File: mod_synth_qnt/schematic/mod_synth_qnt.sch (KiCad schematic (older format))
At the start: 37 parts, among them J1 CV IN, J2 Conn_02x08_Odd_Even, J3 QUANTIZE OUT, J4 Conn_01x07_Male, J5 Conn_01x07_Female, J6 Conn_01x07_Female, J7 Conn_01x07_Male, U1 LM358

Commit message: Use 3mm LEDs for panel hole clearance
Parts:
- D10, D11, D12, D13, D2, D3, D4, D5, D6, D7, D8, D9: footprint LED_THT:LED_D5.0mm -> LED_THT:LED_D3.0mm
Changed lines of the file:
@@
 F 0 "D2" V 8272 2779 50  0000 L CNN
 F 1 "LED 3" V 8363 2779 50  0000 L CNN
-F 2 "LED_THT:LED_D5.0mm" H 8325 2700 50  0001 C CNN
+F 2 "LED_THT:LED_D3.0mm" H 8325 2700 50  0001 C CNN
 F 3 "~" H 8325 2700 50  0001 C CNN
 	1    8325 2700
@@
 F 0 "D3" V 8272 3304 50  0000 L CNN
 F 1 "LED 7" V 8363 3304 50  0000 L CNN
-F 2 "LED_THT:LED_D5.0mm" H 8325 3225 50  0001 C CNN
+F 2 "LED_THT:LED_D3.0mm" H 8325 3225 50  0001 C CNN
 F 3 "~" H 8325 3225 50  0001 C CNN
 	1    8325 3225
@@
 F 0 "D4" V 8272 3829 50  0000 L CNN
 F 1 "LED 11" V 8363 3829 50  0000 L CNN
-F 2 "LED_THT:LED_D5.0mm" H 8325 3750 50  0001 C CNN
+F 2 "LED_THT:LED_D3.0mm" H 8325 3750 50  0001 C CNN
 F 3 "~" H 8325 3750 50  0001 C CNN
 	1    8325 3750
@@
 F 0 "D8" V 8972 2779 50  0000 L CNN
 F 1 "LED 6" V 9063 2779 50  0000 L CNN
-F 2 "LED_THT:LED_D5.0mm" H 9025 2700 50  0001 C CNN
+F 2 "LED_THT:LED_D3.0mm" H 9025 2700 50  0001 C CNN
 F 3 "~" H 9025 2700 50  0001 C CNN
 	1    9025 2700
@@
 F 0 "D10" V 9547 3804 50  0000 L CNN
 F 1 "LED 10" V 9638 3804 50  0000 L CNN
-F 2 "LED_THT:LED_D5.0mm" H 9600 3725 50  0001 C CNN
+F 2 "LED_THT:LED_D3.0mm" H 9600 3725 50  0001 C CNN
 F 3 "~" H 9600 3725 50  0001 C CNN
 	1    9600 3725
@@
 F 0 "D12" V 10022 3304 50  0000 L CNN
 F 1 "LED 9" V 10113 3304 50  0000 L CNN
-F 2 "LED_THT:LED_D5.0mm" H 10075 3225 50  0001 C CNN
+F 2 "LED_THT:LED_D3.0mm" H 10075 3225 50  0001 C CNN
 F 3 "~" H 10075 3225 50  0001 C CNN
 	1    10075 3225
@@
 F 0 "D13" V 10514 3107 50  0000 R CNN
 F 1 "LED 2" V 10423 3107 50  0000 R CNN
-F 2 "LED_THT:LED_D5.0mm" H 10475 3225 50  0001 C CNN
+F 2 "LED_THT:LED_D3.0mm" H 10475 3225 50  0001 C CNN
 F 3 "~" H 10475 3225 50  0001 C CNN
 	1    10475 3225
@@
 F 0 "D5" V 8689 2582 50  0000 R CNN
 F 1 "LED 0" V 8598 2582 50  0000 R CNN
-F 2 "LED_THT:LED_D5.0mm" H 8650 2700 50  0001 C CNN
+F 2 "LED_THT:LED_D3.0mm" H 8650 2700 50  0001 C CNN
 F 3 "~" H 8650 2700 50  0001 C CNN
 	1    8650 2700
@@
 F 0 "D6" V 8689 3082 50  0000 R CNN
 F 1 "LED 4" V 8598 3082 50  0000 R CNN
-F 2 "LED_THT:LED_D5.0mm" H 8650 3200 50  0001 C CNN
+F 2 "LED_THT:LED_D3.0mm" H 8650 3200 50  0001 C CNN
 F 3 "~" H 8650 3200 50  0001 C CNN
 	1    8650 3200
@@
 F 0 "D7" V 8689 3657 50  0000 R CNN
 F 1 "LED 8" V 8598 3657 50  0000 R CNN
-F 2 "LED_THT:LED_D5.0mm" H 8650 3775 50  0001 C CNN
+F 2 "LED_THT:LED_D3.0mm" H 8650 3775 50  0001 C CNN
 F 3 "~" H 8650 3775 50  0001 C CNN
 	1    8650 3775
@@
 F 0 "D9" V 9289 2582 50  0000 R CNN
 F 1 "LED 1" V 9198 2582 50  0000 R CNN
-F 2 "LED_THT:LED_D5.0mm" H 9250 2700 50  0001 C CNN
+F 2 "LED_THT:LED_D3.0mm" H 9250 2700 50  0001 C CNN
 F 3 "~" H 9250 2700 50  0001 C CNN
 	1    9250 2700
@@
 F 0 "D11" V 9864 3607 50  0000 R CNN
 F 1 "LED 5" V 9773 3607 50  0000 R CNN
-F 2 "LED_THT:LED_D5.0mm" H 9825 3725 50  0001 C CNN
+F 2 "LED_THT:LED_D3.0mm" H 9825 3725 50  0001 C CNN
 F 3 "~" H 9825 3725 50  0001 C CNN
 	1    9825 3725

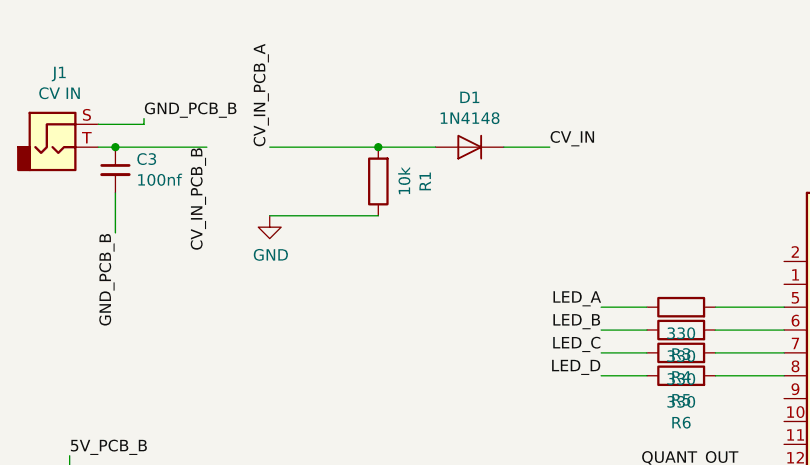
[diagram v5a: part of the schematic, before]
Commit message: Update resistor options
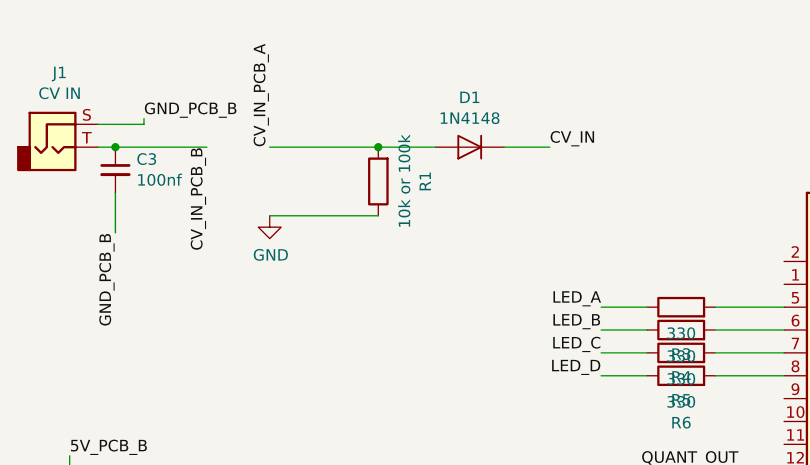
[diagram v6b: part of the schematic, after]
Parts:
- R1: value 10k -> 10k or 100k
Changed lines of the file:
@@
 P 2375 1150
 F 0 "R1" V 2168 1150 50  0000 C CNN
-F 1 "10k" V 2259 1150 50  0000 C CNN
+F 1 "10k or 100k" V 2259 1150 50  0000 C CNN
 F 2 "Resistor_THT:R_Axial_DIN0207_L6.3mm_D2.5mm_P10.16mm_Horizontal" V 2305 1150 50  0001 C CNN
 F 3 "~" H 2375 1150 50  0001 C CNN
